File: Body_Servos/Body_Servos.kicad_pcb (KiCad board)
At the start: 4 copper layers, 80 x 55.1 mm, 38 parts, among them J1 USB_B_Micro, J12 SERIAL_FU, J2 AUX3, J3 AUX1, J4 AUX2, J5 12OUT, J6 12VOUT, J7 5V OUT, J8 5V Out 2, SW1 SW_Push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

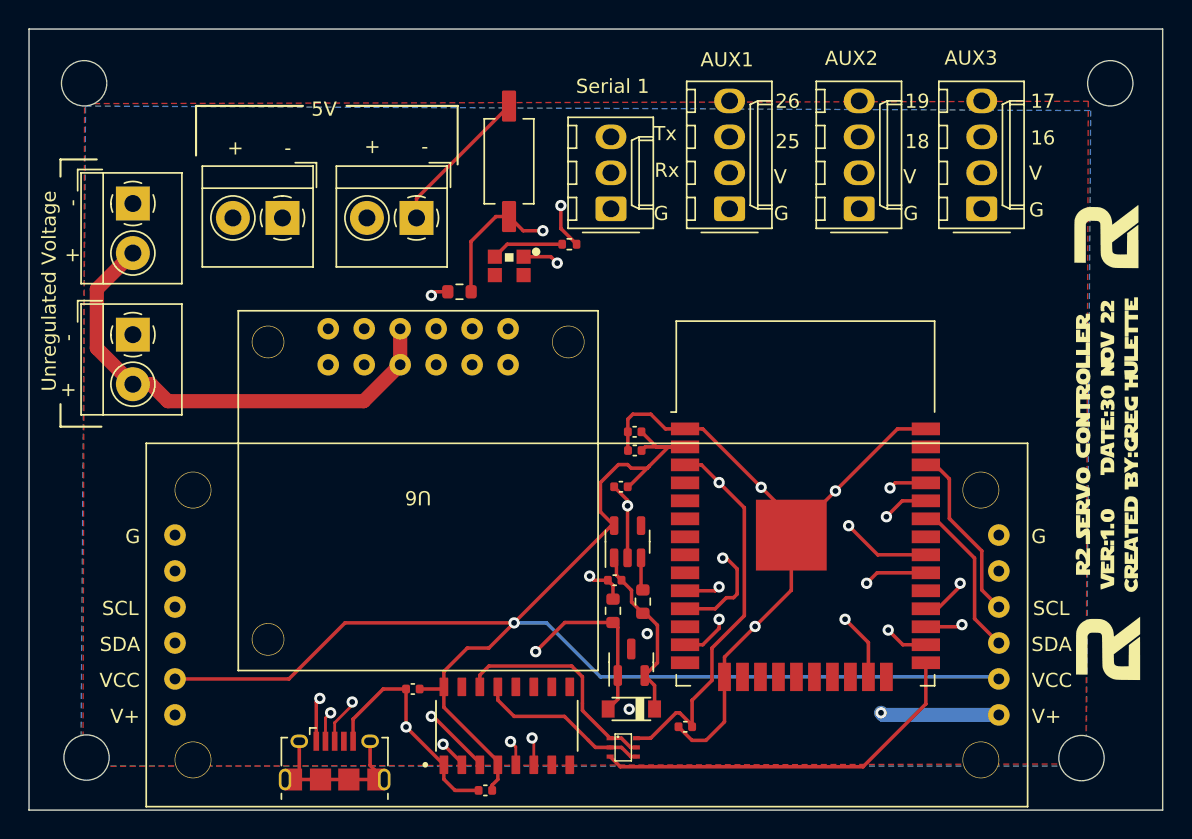
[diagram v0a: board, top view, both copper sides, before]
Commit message: Updated the servo controller to adjust for the 4 pin molex header's alignment pin
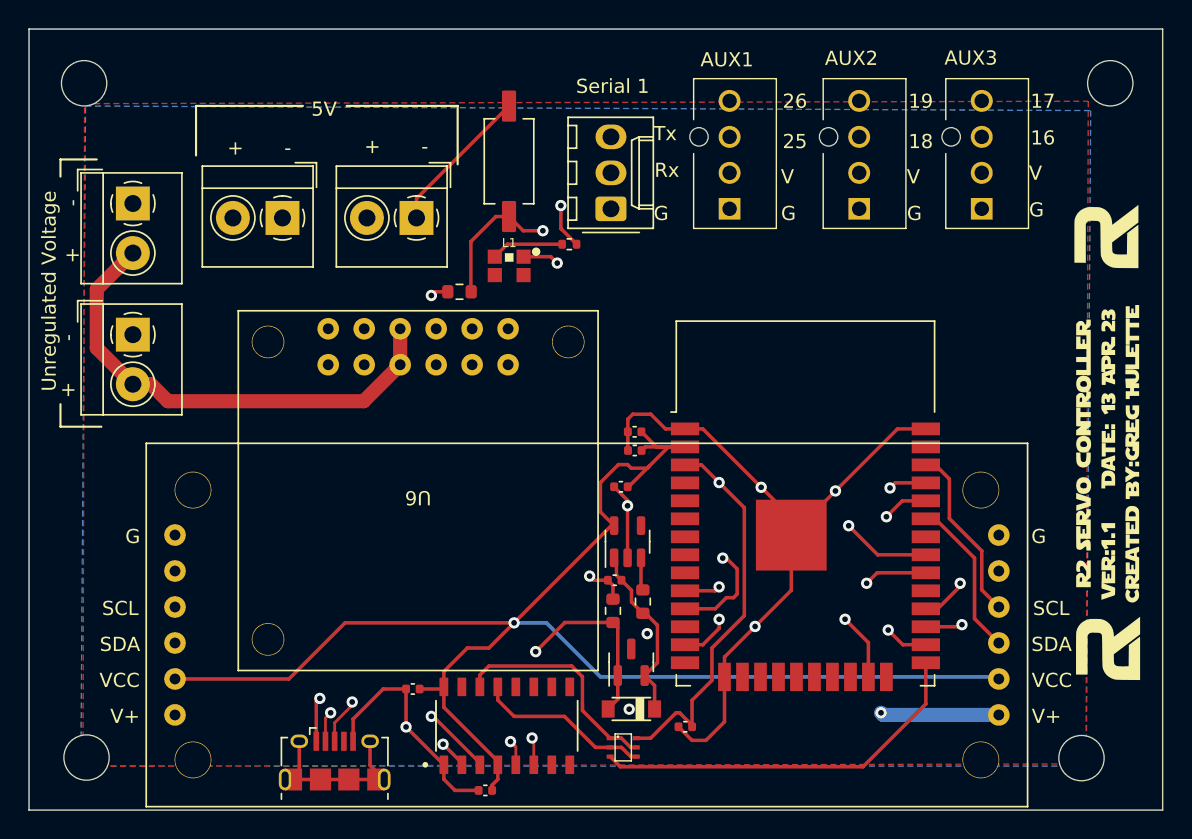
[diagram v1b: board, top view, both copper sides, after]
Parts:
- removed the G*** at (134.8, 110.6)
- added G***: LOGO, Logos:ServoControllerv1.1, F.Cu at (135.1, 111.1)
- J2, J3, J4: footprint Connector_Molex:Molex_KK-254_AE-6410-04A_1x04_P2.54mm_Vertical -> Custom:470531000
- turned J2 to -90 degrees
- turned J3 to -90 degrees
- turned J4 to -90 degrees
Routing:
- net AUX1-2: track 57.4 -> 58.4 mm
